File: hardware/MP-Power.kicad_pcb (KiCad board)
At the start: 2 copper layers, 22.5 x 21 mm, 12 parts, among them U1 MP1584EN

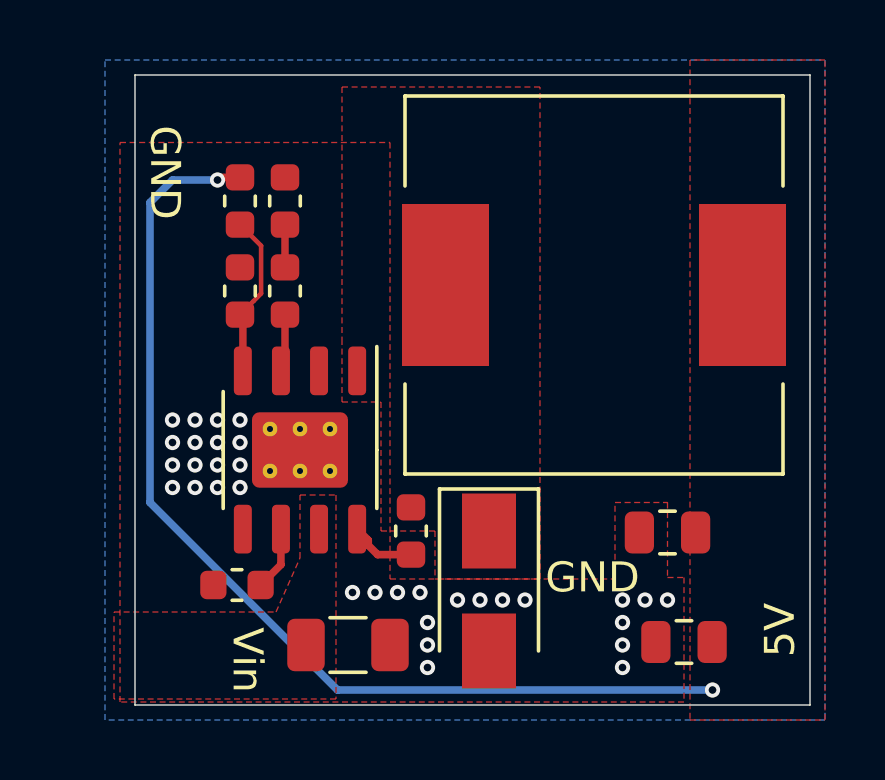
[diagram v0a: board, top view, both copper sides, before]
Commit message: Update inductor for the MP1584 power supply.
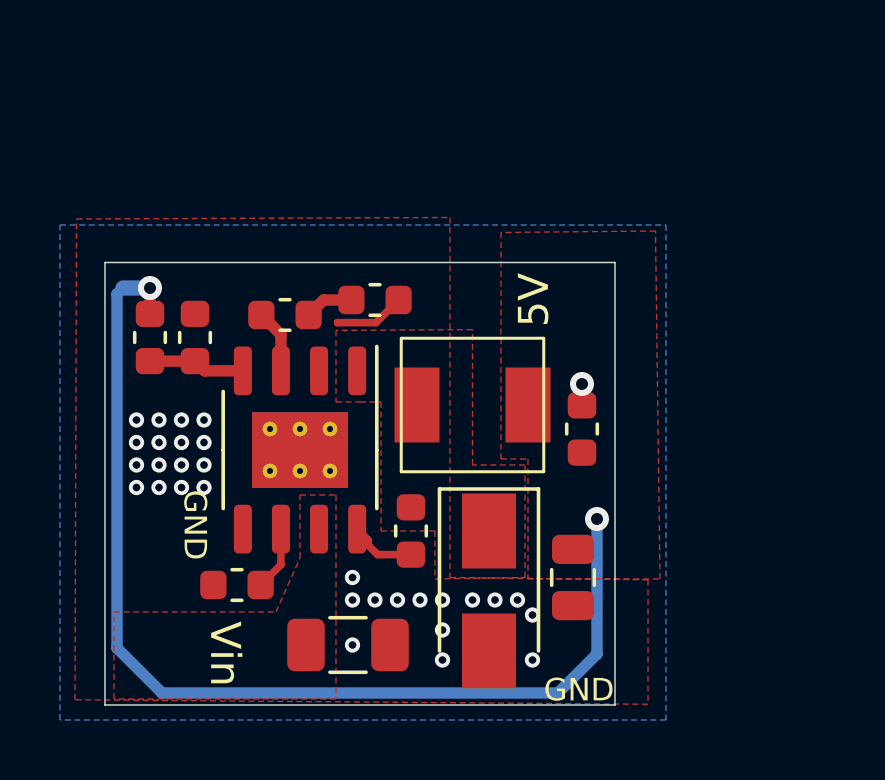
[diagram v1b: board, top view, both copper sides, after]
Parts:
- C5: footprint Capacitor_SMD:C_0805_2012Metric -> Capacitor_SMD:C_0603_1608Metric
- L1: value 15uH -> 10uH; footprint Inductor_SMD:L_12x12mm_H6mm -> PrntrBoardV2:MWSA0402S
- moved L1 5.69 mm to (119.8, 77.0)
- moved R3 5.45 mm to (109.0, 74.8)
- moved C5 4.47 mm to (123.4, 77.8), turned to 90 degrees
- moved R2 4.46 mm to (116.5, 73.5), turned to 0 degrees
- moved C4 4.28 mm to (123.1, 82.8), turned to 270 degrees
- moved R4 2.16 mm to (110.5, 74.8)
- moved C3 0.80 mm to (113.5, 74.0), turned to 0 degrees
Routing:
- net GND: track 0.00 -> 3.06 mm, vias 33 -> 31
- net Net-(R3-Pad2): track 5.50 -> 3.23 mm
- net /5V: track 34.7 -> 35.5 mm
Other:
- board size 22.5 x 21 mm -> 17 x 14.8 mm
- board text added: "(c) iQury.us Nov 2019"
- board text added: "5V Pwr"
- board text added: "rev2"
